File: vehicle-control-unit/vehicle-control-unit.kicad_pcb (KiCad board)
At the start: 2 copper layers, 175.3 x 50.8 mm, 0 parts

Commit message: Route PCB
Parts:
- added C1: 10u, Capacitor_THT:CP_Radial_D5.0mm_P2.50mm, F.Cu at (200.0, 115.6)
- added C2: 10u, Capacitor_THT:CP_Radial_D5.0mm_P2.50mm, F.Cu at (193.7, 115.6)
- added C3: 10u, Capacitor_THT:CP_Radial_D5.0mm_P2.50mm, F.Cu at (185.4, 104.7)
- added C4: 10u, Capacitor_THT:CP_Radial_D5.0mm_P2.50mm, F.Cu at (217.8, 102.3)
- added C5: 10u, Capacitor_THT:CP_Radial_D5.0mm_P2.50mm, F.Cu at (90.8, 92.1)
- added C6: 22u, Capacitor_THT:CP_Radial_D5.0mm_P2.50mm, F.Cu at (108.0, 92.1)
- added C7: 100n, Capacitor_THT:C_Disc_D5.0mm_W2.5mm_P5.00mm, F.Cu at (126.4, 102.2)
- added J1: Conn_02x04_Male_UnitPerRow, Connector_PinHeader_2.54mm:PinHeader_2x04_P2.54mm_Horizontal, F.Cu at (205.1, 114.3)
- added J10: Connector:Screw_Terminal_01x02, TerminalBlock:TerminalBlock_bornier-2_P5.08mm, F.Cu at (82.5, 88.3)
- added J2: Conn_01x04_Male, Connector_PinHeader_2.54mm:PinHeader_1x04_P2.54mm_Horizontal, F.Cu at (193.0, 111.8)
- added J3: Conn_02x03_Male, Connector_PinHeader_2.54mm:PinHeader_2x03_P2.54mm_Horizontal, F.Cu at (160.0, 114.3)
- added J4: Conn_02x03_Male, Connector_PinHeader_2.54mm:PinHeader_2x03_P2.54mm_Horizontal, F.Cu at (150.5, 114.3)
- added J5: Conn_02x03_Male, Connector_PinHeader_2.54mm:PinHeader_2x03_P2.54mm_Horizontal, F.Cu at (169.5, 114.3)
- added J6: Conn_02x03_Male, Connector_PinHeader_2.54mm:PinHeader_2x03_P2.54mm_Horizontal, F.Cu at (179.1, 114.3)
- added J7: Conn_01x03_Male, Connector_PinHeader_2.54mm:PinHeader_1x03_P2.54mm_Horizontal, F.Cu at (105.4, 116.2)
- added J8: Conn_01x03_Male, Connector_PinHeader_2.54mm:PinHeader_1x03_P2.54mm_Horizontal, F.Cu at (88.9, 116.2)
- added J9: Conn_02x06_Male_UnitPerRow, Connector_PinHeader_2.54mm:PinHeader_2x06_P2.54mm_Horizontal, F.Cu at (141.0, 114.3)
- added JP1: Jumper_3_Bridged12, Connector_PinHeader_2.54mm:PinHeader_1x03_P2.54mm_Vertical, F.Cu at (168.9, 109.9)
- added JP2: Jumper_3_Bridged12, Connector_PinHeader_2.54mm:PinHeader_1x03_P2.54mm_Vertical, F.Cu at (163.8, 109.9)
- added JP3: Jumper_3_Bridged12, Connector_PinHeader_2.54mm:PinHeader_1x03_P2.54mm_Vertical, F.Cu at (179.1, 109.9)
- added JP4: Jumper_3_Bridged12, Connector_PinHeader_2.54mm:PinHeader_1x03_P2.54mm_Vertical, F.Cu at (174.0, 109.9)
- added JP5: Jumper_2_Open, Connector_PinHeader_2.54mm:PinHeader_1x02_P2.54mm_Vertical, F.Cu at (148.0, 88.9)
- added JP6: Jumper_3_Bridged12, Connector_PinHeader_2.54mm:PinHeader_1x03_P2.54mm_Vertical, F.Cu at (80.6, 100.3)
- added Q1: BC517, Package_TO_SOT_THT:TO-92_Inline, F.Cu at (80.6, 109.9)
- added R1: 10k, Resistor_THT:R_Axial_DIN0207_L6.3mm_D2.5mm_P10.16mm_Horizontal, F.Cu at (223.5, 108.6)
- added R10: 330E, Resistor_THT:R_Axial_DIN0207_L6.3mm_D2.5mm_P10.16mm_Horizontal, F.Cu at (114.3, 116.2)
- added R11: 470E, Resistor_THT:R_Axial_DIN0207_L6.3mm_D2.5mm_P10.16mm_Horizontal, F.Cu at (146.7, 110.5)
- added R12: 150E, Resistor_THT:R_Axial_DIN0207_L6.3mm_D2.5mm_P10.16mm_Horizontal, F.Cu at (140.3, 110.5)
- added R13: 150E, Resistor_THT:R_Axial_DIN0207_L6.3mm_D2.5mm_P10.16mm_Horizontal, F.Cu at (134.0, 110.5)
- added R14: 330E, Resistor_THT:R_Axial_DIN0207_L6.3mm_D2.5mm_P10.16mm_Horizontal, F.Cu at (97.8, 116.2)
- added R15: 82E, Resistor_THT:R_Axial_DIN0207_L6.3mm_D2.5mm_P10.16mm_Horizontal, F.Cu at (143.5, 110.5)
- added R16: 330E, Resistor_THT:R_Axial_DIN0207_L6.3mm_D2.5mm_P10.16mm_Horizontal, F.Cu at (137.2, 110.5)
- added R17: 330E, Resistor_THT:R_Axial_DIN0207_L6.3mm_D2.5mm_P10.16mm_Horizontal, F.Cu at (130.8, 110.5)
- added R18: 820E, Resistor_THT:R_Axial_DIN0207_L6.3mm_D2.5mm_P10.16mm_Horizontal, F.Cu at (112.4, 92.1)
- added R19: 10k, Resistor_THT:R_Axial_DIN0207_L6.3mm_D2.5mm_P10.16mm_Horizontal, F.Cu at (85.1, 102.9)
- added R2: 10k, Resistor_THT:R_Axial_DIN0207_L6.3mm_D2.5mm_P10.16mm_Horizontal, F.Cu at (226.7, 108.6)
- added R20: 240E, Resistor_THT:R_Axial_DIN0207_L6.3mm_D2.5mm_P10.16mm_Horizontal, F.Cu at (115.6, 81.9)
- added R21: 270k, 1%, Resistor_THT:R_Axial_DIN0207_L6.3mm_D2.5mm_P10.16mm_Horizontal, F.Cu at (120.0, 108.0)
- added R22: 100k, 1%, Resistor_THT:R_Axial_DIN0207_L6.3mm_D2.5mm_P10.16mm_Horizontal, F.Cu at (123.2, 106.0)
- added R3: 10k, Resistor_THT:R_Axial_DIN0207_L6.3mm_D2.5mm_P10.16mm_Horizontal, F.Cu at (217.2, 108.6)
- added R4: 10k, Resistor_THT:R_Axial_DIN0207_L6.3mm_D2.5mm_P10.16mm_Horizontal, F.Cu at (220.3, 108.6)
- added R5: 10k, Resistor_THT:R_Axial_DIN0207_L6.3mm_D2.5mm_P10.16mm_Horizontal, F.Cu at (167.6, 91.4)
- added R6: 10E, Resistor_THT:R_Axial_DIN0207_L6.3mm_D2.5mm_P10.16mm_Horizontal, F.Cu at (101.6, 116.2)
- added R7: 10E, Resistor_THT:R_Axial_DIN0207_L6.3mm_D2.5mm_P10.16mm_Horizontal, F.Cu at (85.1, 116.2)
- added R8: 10k, Resistor_THT:R_Axial_DIN0207_L6.3mm_D2.5mm_P10.16mm_Horizontal, F.Cu at (76.2, 106.0)
- added R9: 100k, Resistor_THT:R_Axial_DIN0207_L6.3mm_D2.5mm_P10.16mm_Horizontal, F.Cu at (73.0, 106.0)
- added RV1: 100E, Potentiometer_THT:Potentiometer_Bourns_3296W_Vertical, F.Cu at (108.0, 85.1)
- added SW1: SW_SPST, Connector_PinHeader_2.54mm:PinHeader_1x02_P2.54mm_Horizontal, F.Cu at (73.0, 101.6)
- added U1: Teensy3.2, earth-rover-footprints:Teensy_3.2, F.Cu at (168.9, 88.9)
- added U2: NRF24L01+ breakout, RF_Module:nRF24L01_Breakout, F.Cu at (223.5, 104.8)
- added U3: ULN2803A, Package_DIP:DIP-18_W7.62mm, F.Cu at (140.3, 81.9)
- added U4: MIC29502WT, Package_TO_SOT_THT:TO-220-5_P3.4x3.8mm_StaggerEven_Lead7.13mm_TabDown, F.Cu at (96.3, 95.9)
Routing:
- net GND: track 0.00 -> 515.8 mm
- net +3V3: track 0.00 -> 172.4 mm
- net +BATT: track 0.00 -> 148.6 mm
- net +5V: track 0.00 -> 123.7 mm
- net /HEADLAMPS: track 0.00 -> 120.2 mm
- net /BEC: track 0.00 -> 106.6 mm, vias 0 -> 2
- net /NRF24L01_MISO: track 0.00 -> 89.3 mm
- net /NRF24L01_SCK: track 0.00 -> 87.4 mm, vias 0 -> 1
- net /NRF24L01_MOSI: track 0.00 -> 83.2 mm, vias 0 -> 1
- net /NRF24L01_IRQ: track 0.00 -> 80.5 mm
- net /NRF24L01_CSN: track 0.00 -> 80.3 mm, vias 0 -> 1
- net /IMU_I2C_SCL: track 0.00 -> 78.8 mm
- net /NRF24L01_CE: track 0.00 -> 78.3 mm, vias 0 -> 1
- net /ENCODER_B: track 0.00 -> 77.2 mm, vias 0 -> 1
- net /IMU_I2C_SDA: track 0.00 -> 76.6 mm
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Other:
- outline, holes or cut-outs redrawn
- net class Default: trace_width 0.25 -> 0.2; via_dia 0.8 -> 0.6; via_drill 0.4 -> 0.35
- rule trace_min: 0.2 -> 0.15
- rule via_min_drill: 0.3 -> 0.35
- rule via_min_size: 0.4 -> 0.6
- board text added: "RC Volvo C202 VCU"
- board text removed: "RC Volvo C202"

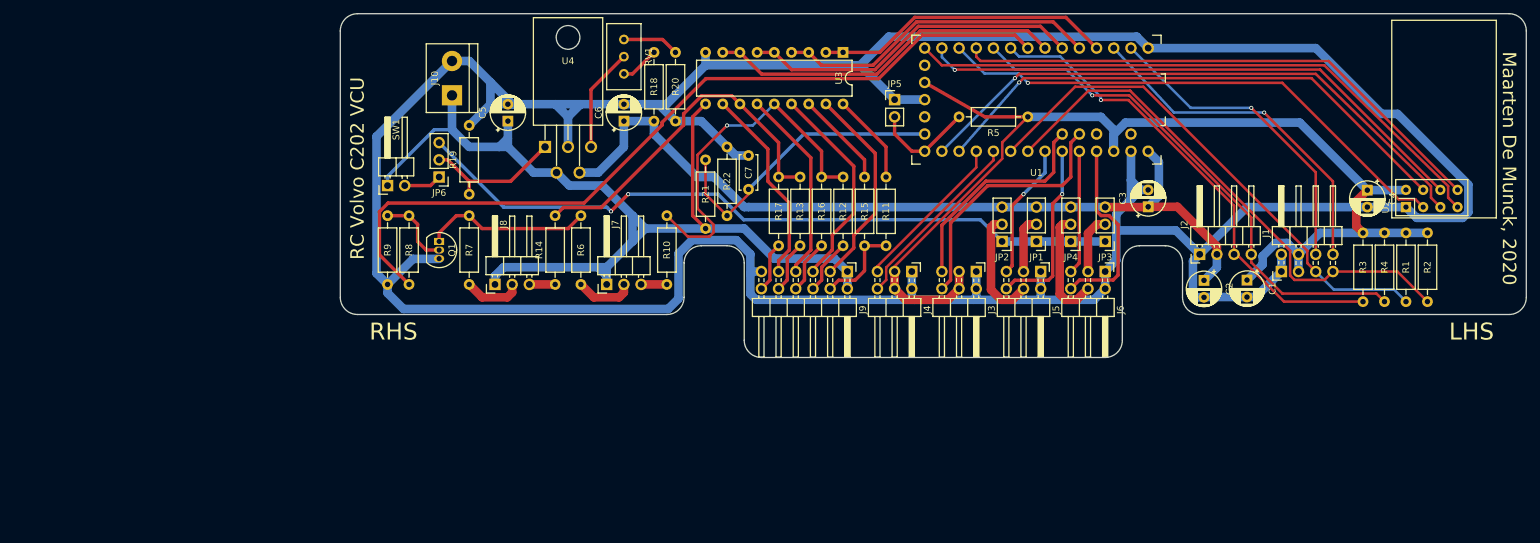
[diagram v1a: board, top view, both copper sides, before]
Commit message: Clean up routing
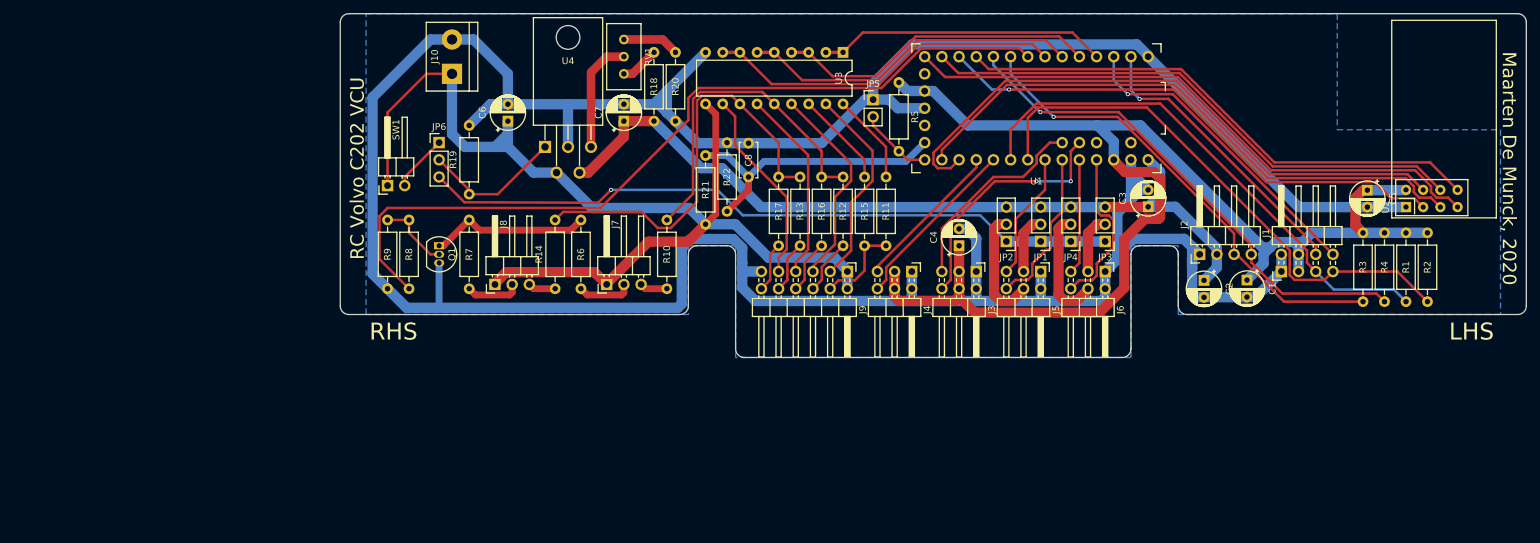
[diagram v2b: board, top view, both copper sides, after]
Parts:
- added C4: 10u, Capacitor_THT:CP_Radial_D5.0mm_P2.50mm, F.Cu at (157.5, 110.5)
- moved R5 19.7 mm to (148.6, 86.4), turned to 270 degrees
- moved JP6 5.08 mm to (80.6, 95.2), turned to 0 degrees
- moved JP5 3.18 mm to (144.8, 88.9)
- moved J10 3.17 mm to (82.5, 85.1)
- moved C8 1.83 mm to (126.4, 100.3)
- moved U1 1.27 mm to (168.9, 90.2)
- moved R10 0.64 mm to (114.3, 116.8)
- moved R14 0.64 mm to (97.8, 116.8)
- moved R21 0.64 mm to (120.0, 107.3)
- moved R22 0.64 mm to (123.2, 105.4)
- moved R6 0.64 mm to (101.6, 116.8)
- moved R7 0.64 mm to (85.1, 116.8)
- moved R8 0.64 mm to (76.2, 106.7)
- moved R9 0.64 mm to (73.0, 106.7)
- moved JP1 0.63 mm to (169.5, 109.9)
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- renumbered C4 to C5, C5 to C6, C6 to C7, C7 to C8
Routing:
- net GND: track 515.8 -> 474.4 mm
- net +3V3: track 172.4 -> 196.4 mm
- net +BATT: track 148.6 -> 163.0 mm
- net Net-(R13-Pad2): track 52.5 -> 62.5 mm
- net /NRF24L01_CSN: track 80.3 -> 89.6 mm, vias 1 -> 0
- net /GPS_SERIAL_RX: track 51.5 -> 46.5 mm
- net /RESET_EEPROM: track 15.2 -> 11.0 mm
- net /GPS_SERIAL_TX: track 47.0 -> 43.0 mm
- net +5V: track 123.7 -> 119.8 mm
- net /WINCH: track 28.1 -> 24.7 mm
- net /THROTTLE: track 26.6 -> 23.8 mm, vias 1 -> 0
- net Net-(JP6-Pad1): track 5.61 -> 8.45 mm
- net /SENSOR_2: track 32.8 -> 30.1 mm
- net Net-(R10-Pad2): track 52.2 -> 49.5 mm, vias 1 -> 0
- net /BEC: track 106.6 -> 103.9 mm, vias 2 -> 1
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- added copper zone on B.Cu, net GND
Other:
- outline, holes or cut-outs redrawn
- rule trace_min: 0.15 -> 0.2

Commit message: Finish VCU PCB
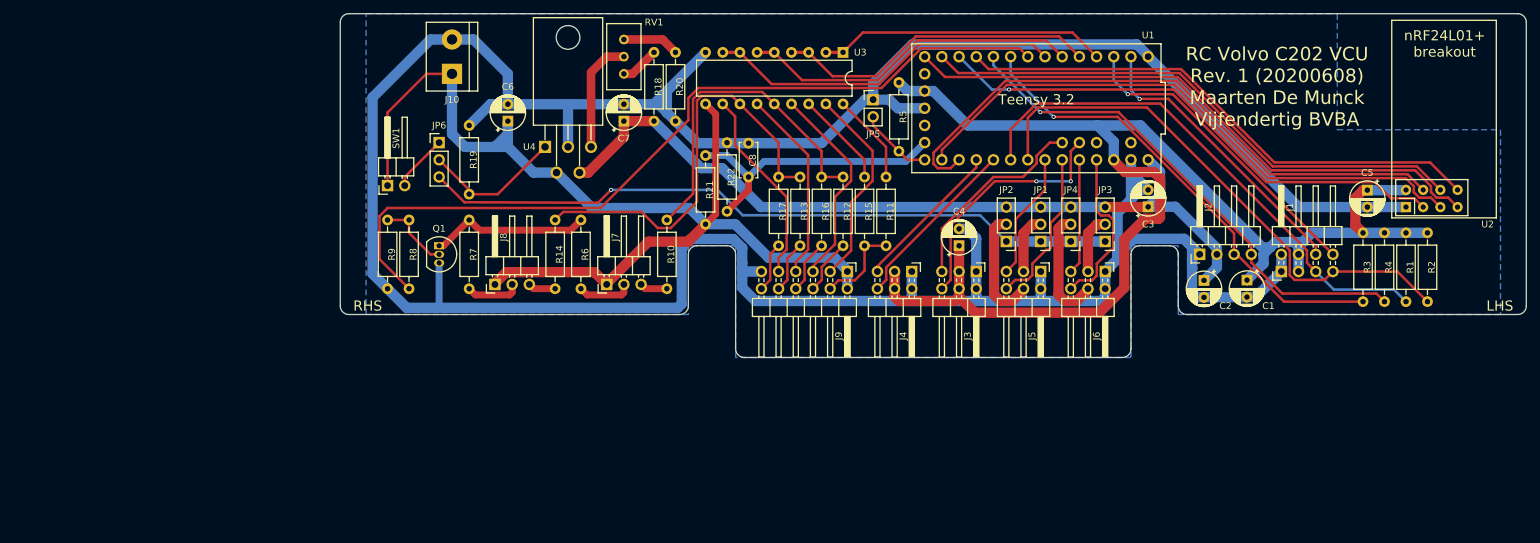
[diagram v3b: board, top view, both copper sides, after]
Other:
- board text added: "RC Volvo C202 VCU Rev. 1 (20200608) Maarten De Munck Vijfendertig BVBA"
- board text added: "Teensy 3.2"
- board text added: "nRF24L01+ breakout"
- board text removed: "Maarten De Munck, 2020"
- board text removed: "RC Volvo C202 VCU"

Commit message: Improve ground plane of VCU PCB
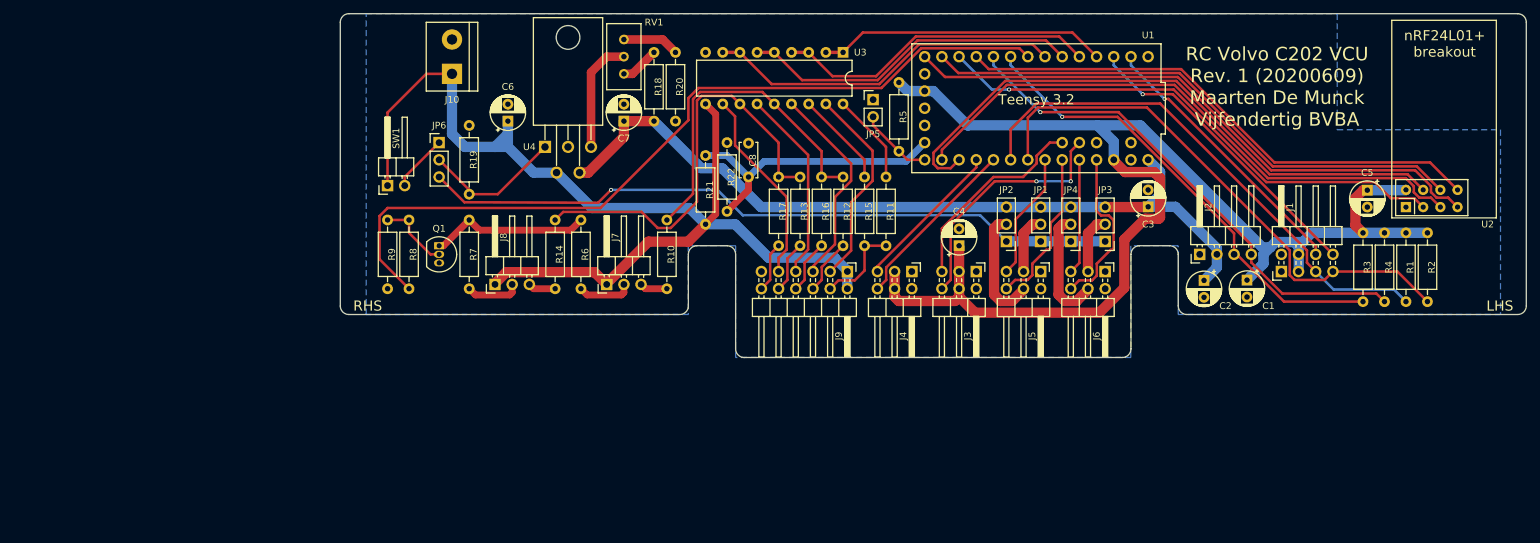
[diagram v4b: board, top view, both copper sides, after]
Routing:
- net GND: track 474.4 -> 0.00 mm
- net /GPS_SERIAL_TX: track 43.0 -> 40.9 mm
- net /GPS_SERIAL_RX: track 46.5 -> 45.2 mm
- net /ENCODER_A: track 70.4 -> 69.6 mm
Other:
- board text added: "RC Volvo C202 VCU Rev. 1 (20200609) Maarten De Munck Vijfendertig BVBA"
- board text removed: "RC Volvo C202 VCU Rev. 1 (20200608) Maarten De Munck Vijfendertig BVBA"

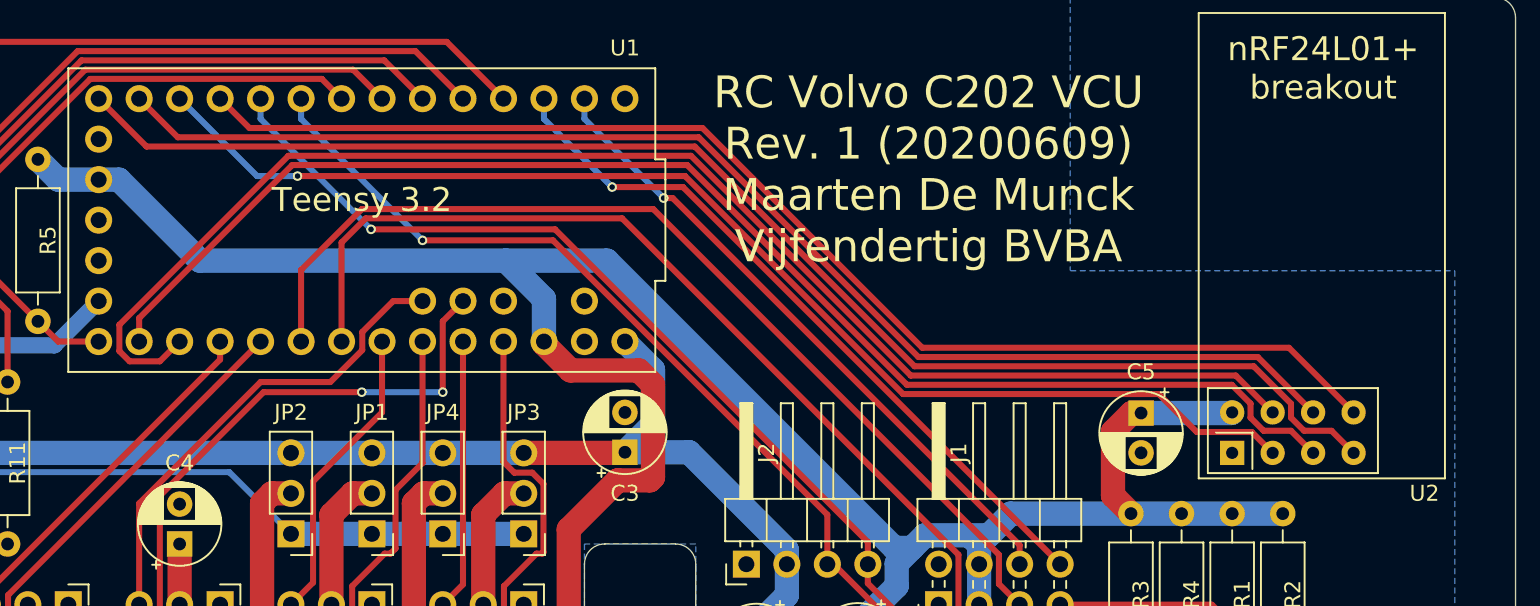
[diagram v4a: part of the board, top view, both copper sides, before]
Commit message: Use larger holes for nRF24L01+ breakout board
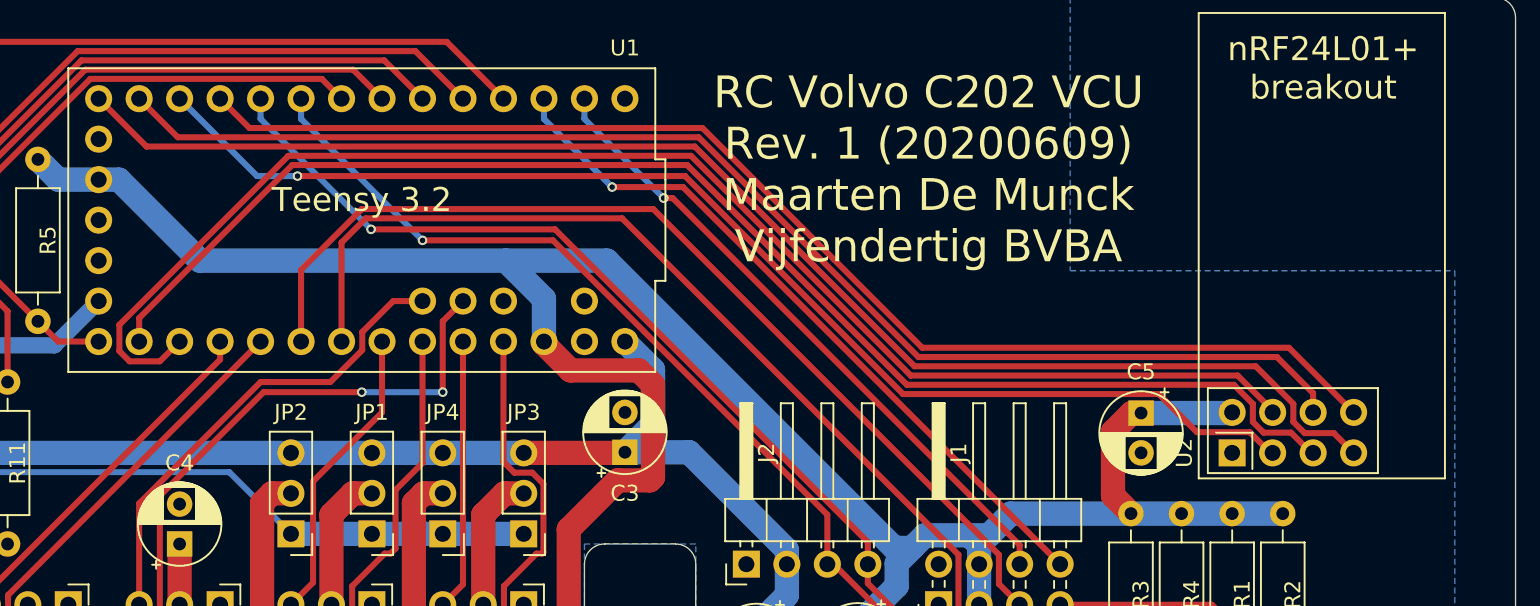
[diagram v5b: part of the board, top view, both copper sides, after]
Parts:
- U2: footprint RF_Module:nRF24L01_Breakout -> earth-rover-footprints:nRF24L01_Breakout_LargerHoles
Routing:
- net /NRF24L01_MOSI: track 81.8 -> 82.5 mm

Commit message: Change value of rear turn signal resistors
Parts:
- R12, R13: value 150E -> 180E
